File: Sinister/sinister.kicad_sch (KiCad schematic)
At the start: 436 parts, among them J1 TYPE-C-31-M12_13, J2 Conn_ARM_JTAG_SWD_10, Q1 AO3401A, Q2 DTC123JKAT146, Q3 DTC123JKAT146, Q4 AO3401A, SW1 MINUS, SW10 4, SW11 5, SW12 6, SW13 7, SW14 8, SW15 9, SW16 0, SW17 MINUS, SW18 PLUS, SW19 BKSP, SW2 FSLASH, SW20 NUM 7, SW21 NUM 8, SW22 NUM 9, SW23 END, SW24 TAB, SW25 Q, SW26 W, SW27 E, SW28 R, SW29 T, SW3 ASTERISK, SW30 Y, SW31 U, SW32 I, SW33 O, SW34 P, SW35 LBRKT, SW36 RBRKT, SW37 BSLASH, SW38 NUM PLUS, SW39 NUM4, SW4 NUM LOCK, SW40 NUM5, SW41 NUM 6, SW42 DEL, SW43 CAPSLOCK, SW44 A, SW45 S, SW46 D, SW47 F, SW48 G, SW49 H, SW5 HOME, SW50 J, SW51 K, SW52 L, SW53 COLON, SW54 QUOTE, SW55 ENTER, SW56 NUM 1, SW57 NUM 2, SW58 NUM 3, SW59 UP, SW6 ESC, SW60 LSHIFT, SW61 Z, SW62 X, SW63 C, SW64 V, SW65 B, SW66 N, SW67 M, SW68 COMMA, SW69 PERIOD, SW7 1, SW70 FSLASH, SW71 RSHIFT, SW72 NUM ENTER, SW73 NUM PERIOD, SW74 NUM 0, SW75 LEFT, SW76 DOWN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

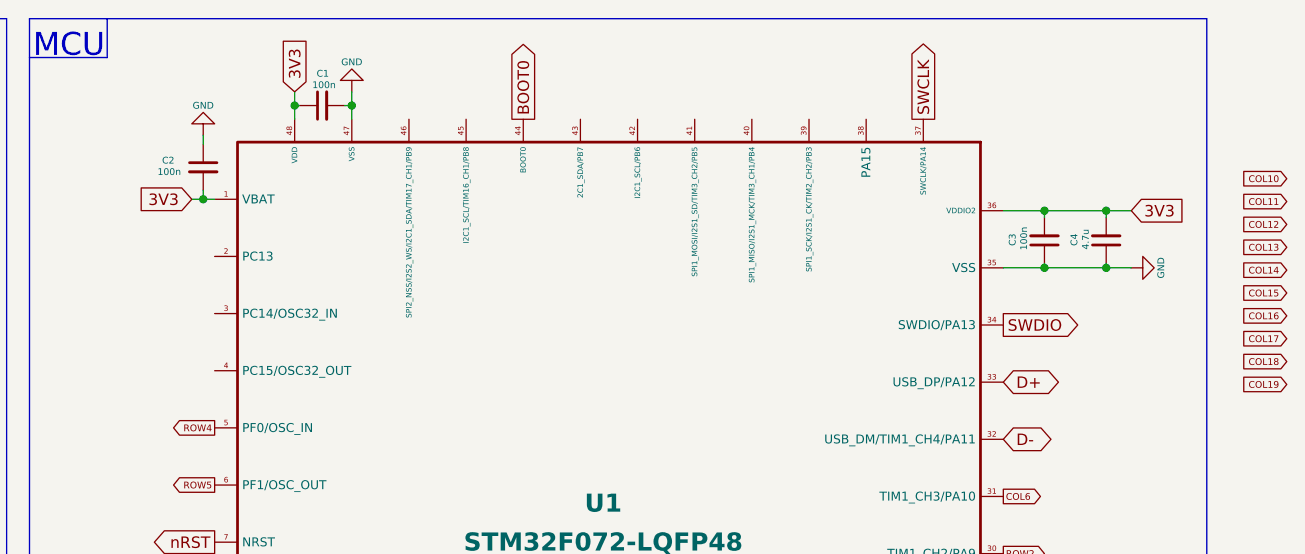
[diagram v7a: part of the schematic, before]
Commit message: Finished routing tracks, Ran DRC, resolved errors.
Finished routing the final 10 columns to the MCU. Ran DRC and resolved errors. 1 pad size error for USBC and two warnings for unconnected trakcs that are cosmetic are all that remain.
Still to do: Silkscreen.
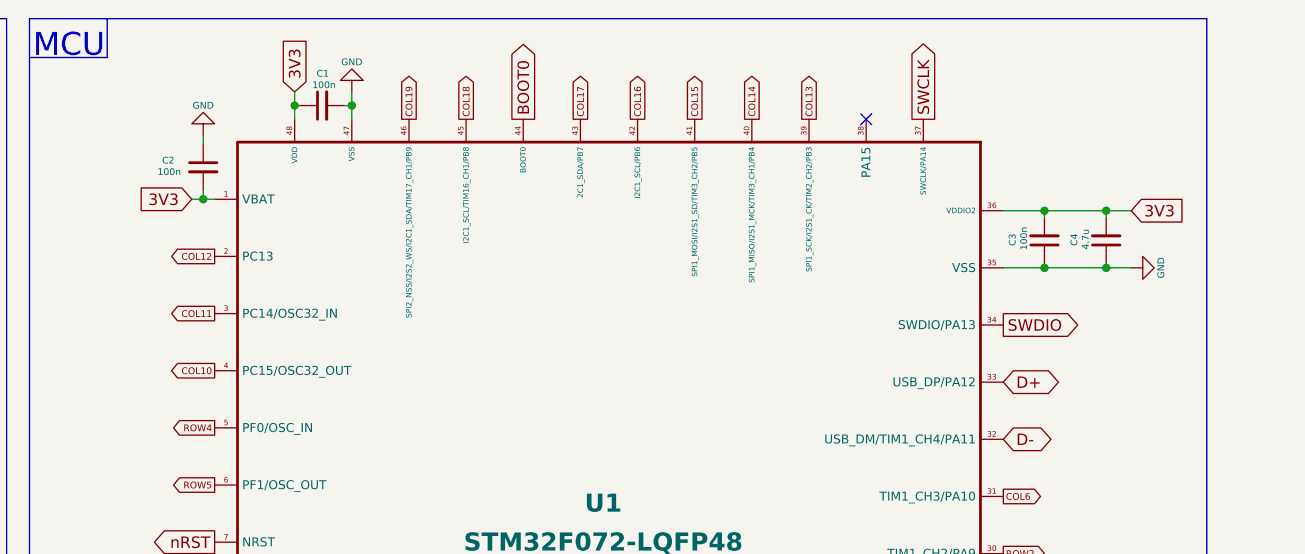
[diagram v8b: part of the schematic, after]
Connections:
- net COL10: now also U1.4 (PC15/OSC32_OUT)
- net COL11: now also U1.3 (PC14/OSC32_IN)
- net COL12: now also U1.2 (PC13)
- net COL13: now also U1.39 (SPI1_SCK/I2S1_CK/TIM2_CH2/PB3)
- net COL14: now also U1.40 (SPI1_MISO/I2S1_MCK/TIM3_CH1/PB4)
- net COL15: now also U1.41 (SPI1_MOSI/I2S1_SD/TIM3_CH2/PB5)
- net COL16: now also U1.42 (I2C1_SCL/PB6)
- net COL17: now also U1.43 (2C1_SDA/PB7)
- net COL18: now also U1.45 (I2C1_SCL/TIM16_CH1/PB8)
- net COL19: now also U1.46 (SPI2_NSS/I2S2_WS/I2C1_SDA/TIM17_CH1/PB9)
- no-connect marks 6 -> 7
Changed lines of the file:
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@@
   (junction (at 528.574 36.576) (diameter 0) (color 0 0 0 0))
   (junction (at 528.574 42.926) (diameter 0) (color 0 0 0 0))
+  (no_connect (at 279.4 233.68))
+  (no_connect (at 279.4 231.14))
+  (no_connect (at 501.904 26.416))
+  (no_connect (at 517.144 100.076))
+  (no_connect (at 227.076 368.046))
+  (no_connect (at 320.04 278.638))
   (no_connect (at 320.04 281.178))
-  (no_connect (at 279.4 231.14))
-  (no_connect (at 279.4 233.68))
-  (no_connect (at 320.04 278.638))
-  (no_connect (at 227.076 368.046))
-  (no_connect (at 517.144 100.076))
   (wire (pts (xy 20.32 334.264) (xy 29.21 334.264))
     (stroke (width 0) (type solid) (color 0 0 0 0))
@@
     (effects (font (size 1.27 1.27)) (justify right))
   )
+  (global_label "COL12" (shape output) (at 429.514 41.656 180)
+    (effects (font (size 0.75 0.75)) (justify right))
+  )
+  (global_label "COL11" (shape output) (at 429.514 48.006 180)
+    (effects (font (size 0.75 0.75)) (justify right))
+  )
+  (global_label "COL10" (shape output) (at 429.514 54.356 180)
+    (effects (font (size 0.75 0.75)) (justify right))
+  )
   (global_label "ROW4" (shape output) (at 429.514 60.706 180)
     (effects (font (size 0.75 0.75)) (justify right))
@@
     (effects (font (size 1.27 1.27)) (justify right))
   )
+  (global_label "COL19" (shape output) (at 451.104 26.416 90)
+    (effects (font (size 0.75 0.75)) (justify left))
+  )
   (global_label "INDICATOR5" (shape output) (at 451.104 114.046 270)
     (effects (font (size 1.27 1.27)) (justify right))
   )
+  (global_label "COL18" (shape output) (at 457.454 26.416 90)
+    (effects (font (size 0.75 0.75)) (justify left))
+  )
   (global_label "LED_PWM" (shape output) (at 457.454 114.046 270)
     (effects (font (size 1.27 1.27)) (justify right))
@@
     (effects (font (size 0.75 0.75)) (justify right))
   )
+  (global_label "COL17" (shape output) (at 470.154 26.416 90)
+    (effects (font (size 0.75 0.75)) (justify left))
+  )
   (global_label "COL2" (shape output) (at 470.154 114.046 270)
     (effects (font (size 0.75 0.75)) (justify right))
   )
+  (global_label "COL16" (shape output) (at 476.504 26.416 90)
+    (effects (font (size 0.75 0.75)) (justify left))
+  )
   (global_label "COL3" (shape output) (at 476.504 114.046 270)
     (effects (font (size 0.75 0.75)) (justify right))
   )
+  (global_label "COL15" (shape output) (at 482.854 26.416 90)
+    (effects (font (size 0.75 0.75)) (justify left))
+  )
   (global_label "COL4" (shape output) (at 482.854 114.046 270)
     (effects (font (size 0.75 0.75)) (justify right))
   )
+  (global_label "COL14" (shape output) (at 489.204 26.416 90)
+    (effects (font (size 0.75 0.75)) (justify left))
+  )
   (global_label "COL5" (shape output) (at 489.204 114.046 270)
     (effects (font (size 0.75 0.75)) (justify right))
   )
+  (global_label "COL13" (shape output) (at 495.554 26.416 90)
+    (effects (font (size 0.75 0.75)) (justify left))
+  )
   (global_label "ROW3" (shape output) (at 495.554 114.046 270)
     (effects (font (size 0.75 0.75)) (justify right))
@@
     (effects (font (size 1.27 1.27)) (justify left))
   )
-  (global_label "COL10" (shape input) (at 548.64 33.02 180)
-    (effects (font (size 0.75 0.75)) (justify right))
-  )
-  (global_label "COL11" (shape input) (at 548.64 35.56 180)
-    (effects (font (size 0.75 0.75)) (justify right))
-  )
-  (global_label "COL12" (shape input) (at 548.64 38.1 180)
-    (effects (font (size 0.75 0.75)) (justify right))
-  )
-  (global_label "COL13" (shape input) (at 548.64 40.64 180)
-    (effects (font (size 0.75 0.75)) (justify right))
-  )
-  (global_label "COL14" (shape input) (at 548.64 43.18 180)
-    (effects (font (size 0.75 0.75)) (justify right))
-  )
-  (global_label "COL15" (shape input) (at 548.64 45.72 180)
-    (effects (font (size 0.75 0.75)) (justify right))
-  )
-  (global_label "COL16" (shape input) (at 548.64 48.26 180)
-    (effects (font (size 0.75 0.75)) (justify right))
-  )
-  (global_label "COL17" (shape input) (at 548.64 50.8 180)
-    (effects (font (size 0.75 0.75)) (justify right))
-  )
-  (global_label "COL18" (shape input) (at 548.64 53.34 180)
-    (effects (font (size 0.75 0.75)) (justify right))
-  )
-  (global_label "COL19" (shape input) (at 548.64 55.88 180)
-    (effects (font (size 0.75 0.75)) (justify right))
-  )
   (symbol (lib_id "power:GND") (at 20.32 355.854 0) (mirror y) (unit 1)
